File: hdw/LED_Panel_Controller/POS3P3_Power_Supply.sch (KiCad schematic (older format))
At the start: 20 parts

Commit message: made a lot more schematic progress
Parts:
- removed L?: 3.3uH, Inductors_SMD:L_Vishay_IHLP-1212, symbol Custom_Library:L_Custom
- removed U?: TPS62150, Package_DFN_QFN:QFN-16-1EP_3x3mm_P0.5mm_EP1.8x1.8mm, symbol Custom_Library:TPS62150
- added L?: 2.2uH, symbol Custom_Library:L_Custom
- added R? (x3): 0, Resistors_SMD:R_0402, symbol Custom_Library:R_Custom
- added U?: TPS62130, Package_DFN_QFN:QFN-16-1EP_3x3mm_P0.5mm_EP1.8x1.8mm, symbol Custom_Library:TPS62130
- R? (x3): Configuration (none) -> Telemetry
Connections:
- net +12V: now also U?.10 (AVIN), U?.11 (PVIN), U?.12 (PVIN)
- net +3V3: now also R?.2, R?.2, R?.2, U?.14 (VOS)
- net GND: now also U?.15 (PGND), U?.16 (PGND), U?.17 (EP), U?.6 (AGND), U?.7 (FSW), U?.8 (DEF)
- net POS3P3_PGOOD: now also U?.4 (PG)
- net POS3P3_RUN: now also U?.13 (EN)
- net at C?.1, R?.1, R?.2: now also L?.2, R?.1, R?.1, R?.1
- net at R?.1, R?.2: now also U?.5 (FB)
- net at C?.1: now also U?.9 (SS/TR)
- net POS3P3_SNS_OUT+ renamed POS3P3_SNS+
- net POS3P3_SNS_OUT- renamed POS3P3_SNS-
- new net: L?.1, U?.1 (SW), U?.2 (SW), U?.3 (SW)
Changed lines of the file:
@@
 $EndDescr
-$Comp
-L Custom_Library:L_Custom L?
-U 1 1 5C26EF0D
-P 6330 3040
-AR Path="/5CB7718D/5C26EF0D" Ref="L?"  Part="1"
-AR Path="/5E0DC082/5C26EF0D" Ref="L?"  Part="1"
-AR Path="/5E0F263A/5C26EF0D" Ref="L?"  Part="1"
-AR Path="/5EAE2D8A/5C26EF0D" Ref="L?"  Part="1"
-AR Path="/5F581B64/5C26EF0D" Ref="L?"  Part="1"
-F 0 "L?" V 6280 3040 50  0000 C CNN
-F 1 "3.3uH" V 6405 3040 50  0000 C CNN
-F 2 "Inductors_SMD:L_Vishay_IHLP-1212" H 6330 3040 50  0001 C CNN
-F 3 "" H 6330 3040 50  0001 C CNN
-F 4 "541-2567-1-ND" H 6330 3040 50  0001 C CNN "Digi-Key PN"
-F 5 "IHLP1212" V 6480 3040 50  0000 C CNN "display_footprint"
-F 6 "2.7A" V 6580 3040 50  0000 C CNN "Ampacity"
-F 7 "20%" V 6680 3040 50  0000 C CNN "Tolerance"
-	1    6330 3040
-	0    -1   -1   0
-$EndComp
 $Comp
 L Custom_Library:C_Custom C?
@@
 Wire Wire Line
 	5890 3040 6180 3040
-$Comp
-L Custom_Library:R_Custom R?
-U 1 1 5E06F7D6
-P 7520 3040
-AR Path="/5CB6F1ED/5E06F7D6" Ref="R?"  Part="1"
-AR Path="/5CB7718D/5E06F7D6" Ref="R?"  Part="1"
-AR Path="/5E0DC082/5E06F7D6" Ref="R?"  Part="1"
-AR Path="/5E0F263A/5E06F7D6" Ref="R?"  Part="1"
-AR Path="/5EAE2D8A/5E06F7D6" Ref="R?"  Part="1"
-AR Path="/5F581B64/5E06F7D6" Ref="R?"  Part="1"
-F 0 "R?" V 7420 3040 50  0000 C CNN
-F 1 "0.02" V 7520 3040 40  0000 C CNN
-F 2 "Resistors_SMD:R_0612" H 7520 3040 50  0001 C CNN
-F 3 "" H 7520 3040 50  0001 C CNN
-F 4 "P16010CT-ND" H 7820 3440 60  0001 C CNN "Digi-Key PN"
-F 5 "0612" V 7620 3040 50  0000 C CNN "display_footprint"
-F 6 "1%" V 7720 3040 50  0000 C CNN "Tolerance"
-F 7 "1W" V 7820 3040 50  0000 C CNN "Wattage"
-	1    7520 3040
-	0    -1   -1   0
-$EndComp
 Text GLabel 7290 2560 1    50   UnSpc ~ 0
-POS3P3_SNS_OUT+
+POS3P3_SNS+
 Text GLabel 7750 2560 1    50   UnSpc ~ 0
-POS3P3_SNS_OUT-
+POS3P3_SNS-
 Wire Wire Line
 	6480 3040 6920 3040
@@
 F 5 "1%" V 7490 2710 50  0001 C CNN "Tolerance"
 F 6 "1/16W" V 7590 2710 50  0001 C CNN "Wattage"
-F 7 "" H 7290 2710 50  0001 C CNN "Digi-Key PN"
+F 7 "Telemetry" V 7390 2710 50  0000 C CNN "Configuration"
 	1    7290 2710
 	-1   0    0    -1
@@
 F 5 "1%" V 7950 2710 50  0001 C CNN "Tolerance"
 F 6 "1/16W" V 8050 2710 50  0001 C CNN "Wattage"
-F 7 "" H 7750 2710 50  0001 C CNN "Digi-Key PN"
+F 7 "Telemetry" V 7850 2710 50  0000 C CNN "Configuration"
 	1    7750 2710
 	-1   0    0    -1
@@
 Wire Wire Line
 	7290 3040 7370 3040
-Wire Wire Line
-	7750 2860 7750 3040
 Connection ~ 7750 3040
 Wire Wire Line
@@
 	1    0    0    -1
 $EndComp
-$Comp
-L Custom_Library:TPS62150 U?
-U 1 1 5EB8DB31
-P 5390 3740
-F 0 "U?" H 5390 4990 50  0000 C CNN
-F 1 "TPS62150" H 5390 3740 50  0000 C CNN
-F 2 "Package_DFN_QFN:QFN-16-1EP_3x3mm_P0.5mm_EP1.8x1.8mm" H 5390 3740 50  0001 C CNN
-F 3 "https://www.ti.com/lit/ds/symlink/tps62150.pdf?&ts=1589125931316" H 5390 3740 50  0001 C CNN
-F 4 "296-41757-1-ND" H 5290 3740 50  0001 C CNN "Digi-Key PN"
-	1    5390 3740
-	1    0    0    -1
-$EndComp
 Wire Wire Line
 	8220 3960 8220 4240
@@
 Text GLabel 4090 7490 0    50   Input ~ 0
 POS3P3_RUN
+$Comp
+L Custom_Library:TPS62130 U?
+U 1 1 6019E970
+P 5390 3740
+AR Path="/5F581BA3/6019E970" Ref="U?"  Part="1"
+AR Path="/5F581B64/6019E970" Ref="U?"  Part="1"
+F 0 "U?" H 5390 4990 50  0000 C CNN
+F 1 "TPS62130" H 5390 3740 50  0000 C CNN
+F 2 "Package_DFN_QFN:QFN-16-1EP_3x3mm_P0.5mm_EP1.8x1.8mm" H 5390 3740 50  0001 C CNN
+F 3 "http://www.ti.com/lit/ds/symlink/tps62130.pdf" H 5390 3740 50  0001 C CNN
+F 4 "296-37878-1-ND" H 5290 3740 50  0001 C CNN "Digi-Key PN"
+	1    5390 3740
+	1    0    0    -1
+$EndComp
+$Comp
+L Custom_Library:L_Custom L?
+U 1 1 601A324F
+P 6330 3040
+AR Path="/5F581BA3/601A324F" Ref="L?"  Part="1"
+AR Path="/5F581B64/601A324F" Ref="L?"  Part="1"
+F 0 "L?" V 6280 3040 50  0000 C CNN
+F 1 "2.2uH" V 6405 3040 50  0000 C CNN
+F 2 "" H 6330 3040 50  0001 C CNN
+F 3 "" H 6330 3040 50  0001 C CNN
+F 4 "IHLP2020" V 6480 3040 50  0000 C CNN "display_footprint"
+F 5 "6.7A" V 6580 3040 50  0000 C CNN "Ampacity"
+F 6 "20%" V 6680 3040 50  0000 C CNN "Tolerance"
+F 7 "541-1236-1-ND" H 6330 3040 50  0001 C CNN "Digi-Key PN"
+	1    6330 3040
+	0    -1   -1   0
+$EndComp
+$Comp
+L Custom_Library:R_Custom R?
+U 1 1 601AAF61
+P 7520 3410
+AR Path="/5EAE2EF2/601AAF61" Ref="R?"  Part="1"
+AR Path="/5EAE30C7/601AAF61" Ref="R?"  Part="1"
+AR Path="/5EAE2D8A/601AAF61" Ref="R?"  Part="1"
+AR Path="/5EAE2D66/601AAF61" Ref="R?"  Part="1"
+AR Path="/5F581B41/601AAF61" Ref="R?"  Part="1"
+AR Path="/5F581B64/601AAF61" Ref="R?"  Part="1"
+F 0 "R?" V 7420 3410 50  0000 C CNN
+F 1 "0" V 7520 3410 50  0000 C CNN
+F 2 "Resistors_SMD:R_0402" H 7520 3410 50  0001 C CNN
+F 3 "" H 7520 3410 50  0001 C CNN
+F 4 "0402" V 7620 3410 50  0001 C CNN "display_footprint"
+F 5 "1%" V 7720 3410 50  0001 C CNN "Tolerance"
+F 6 "1/16W" V 7820 3410 50  0001 C CNN "Wattage"
+F 7 "~Telemetry" V 7620 3410 50  0000 C CNN "Configuration"
+F 8 "2019-RK73Z1ETTPCT-ND" H 7520 3410 50  0001 C CNN "Digi-Key PN"
+	1    7520 3410
+	0    -1   1    0
+$EndComp
+$Comp
+L Custom_Library:R_Custom R?
+U 1 1 601AAF6C
+P 7520 3710
+AR Path="/5EAE2EF2/601AAF6C" Ref="R?"  Part="1"
+AR Path="/5EAE30C7/601AAF6C" Ref="R?"  Part="1"
+AR Path="/5EAE2D8A/601AAF6C" Ref="R?"  Part="1"
+AR Path="/5EAE2D66/601AAF6C" Ref="R?"  Part="1"
+AR Path="/5F581B41/601AAF6C" Ref="R?"  Part="1"
+AR Path="/5F581B64/601AAF6C" Ref="R?"  Part="1"
+F 0 "R?" V 7420 3710 50  0000 C CNN
+F 1 "0" V 7520 3710 50  0000 C CNN
+F 2 "Resistors_SMD:R_0402" H 7520 3710 50  0001 C CNN
+F 3 "" H 7520 3710 50  0001 C CNN
+F 4 "0402" V 7620 3710 50  0001 C CNN "display_footprint"
+F 5 "1%" V 7720 3710 50  0001 C CNN "Tolerance"
+F 6 "1/16W" V 7820 3710 50  0001 C CNN "Wattage"
+F 7 "~Telemetry" V 7620 3710 50  0000 C CNN "Configuration"
+F 8 "2019-RK73Z1ETTPCT-ND" H 7520 3710 50  0001 C CNN "Digi-Key PN"
+	1    7520 3710
+	0    -1   1    0
+$EndComp
+$Comp
+L Custom_Library:R_Custom R?
+U 1 1 601AAF77
+P 7520 4010
+AR Path="/5EAE2EF2/601AAF77" Ref="R?"  Part="1"
+AR Path="/5EAE30C7/601AAF77" Ref="R?"  Part="1"
+AR Path="/5EAE2D8A/601AAF77" Ref="R?"  Part="1"
+AR Path="/5EAE2D66/601AAF77" Ref="R?"  Part="1"
+AR Path="/5F581B41/601AAF77" Ref="R?"  Part="1"
+AR Path="/5F581B64/601AAF77" Ref="R?"  Part="1"
+F 0 "R?" V 7420 4010 50  0000 C CNN
+F 1 "0" V 7520 4010 50  0000 C CNN
+F 2 "Resistors_SMD:R_0402" H 7520 4010 50  0001 C CNN
+F 3 "" H 7520 4010 50  0001 C CNN
+F 4 "0402" V 7620 4010 50  0001 C CNN "display_footprint"
+F 5 "1%" V 7720 4010 50  0001 C CNN "Tolerance"
+F 6 "1/16W" V 7820 4010 50  0001 C CNN "Wattage"
+F 7 "~Telemetry" V 7620 4010 50  0000 C CNN "Configuration"
+F 8 "2019-RK73Z1ETTPCT-ND" H 7520 4010 50  0001 C CNN "Digi-Key PN"
+	1    7520 4010
+	0    -1   1    0
+$EndComp
+Wire Wire Line
+	7670 4010 7750 4010
+Wire Wire Line
+	7750 4010 7750 3710
+Wire Wire Line
+	7290 4010 7370 4010
+Wire Wire Line
+	7370 3710 7290 3710
+Connection ~ 7290 3710
+Wire Wire Line
+	7290 3710 7290 4010
+Wire Wire Line
+	7670 3710 7750 3710
+Connection ~ 7750 3710
+Wire Wire Line
+	7750 3710 7750 3410
+Wire Wire Line
+	7670 3410 7750 3410
+Connection ~ 7750 3410
+Wire Wire Line
+	7370 3410 7290 3410
+Connection ~ 7290 3410
+Wire Wire Line
+	7290 3410 7290 3710
+Wire Wire Line
+	7750 2860 7750 3040
+$Comp
+L Custom_Library:R_Custom R?
+U 1 1 5E06F7D6
+P 7520 3040
+AR Path="/5CB6F1ED/5E06F7D6" Ref="R?"  Part="1"
+AR Path="/5CB7718D/5E06F7D6" Ref="R?"  Part="1"
+AR Path="/5E0DC082/5E06F7D6" Ref="R?"  Part="1"
+AR Path="/5E0F263A/5E06F7D6" Ref="R?"  Part="1"
+AR Path="/5EAE2D8A/5E06F7D6" Ref="R?"  Part="1"
+AR Path="/5F581B64/5E06F7D6" Ref="R?"  Part="1"
+F 0 "R?" V 7420 3040 50  0000 C CNN
+F 1 "0.02" V 7520 3040 40  0000 C CNN
+F 2 "Resistors_SMD:R_0612" H 7520 3040 50  0001 C CNN
+F 3 "" H 7520 3040 50  0001 C CNN
+F 4 "P16010CT-ND" H 7820 3440 60  0001 C CNN "Digi-Key PN"
+F 5 "0612" V 7620 3040 50  0000 C CNN "display_footprint"
+F 6 "1%" V 7720 3040 50  0000 C CNN "Tolerance"
+F 7 "1W" V 7820 3040 50  0000 C CNN "Wattage"
+F 8 "Telemetry" V 7350 3040 50  0000 C CNN "Configuration"
+	1    7520 3040
+	0    -1   -1   0
+$EndComp
+Wire Wire Line
+	7290 3040 7290 3410
+Wire Wire Line
+	7750 3040 7750 3410
 $EndSCHEMATC

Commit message: more schematic development
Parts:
- removed C?: 100uF, Capacitors_SMD:C_1206, symbol Custom_Library:C_Custom
- removed C?: 0.1uF, Capacitors_SMD:C_0402, symbol Custom_Library:C_Custom
- removed C?: 10uF, Capacitors_SMD:C_0402, symbol Custom_Library:C_Custom
- removed D?: BAT48JFILM, Diode_SMD:D_SOD-323, symbol Diode:BAT48JFILM
- removed L?: 2.2uH, symbol Custom_Library:L_Custom
- removed Q?: ZXMS6004FFTA, Package_TO_SOT_SMD:SOT-23, symbol Custom_Library:ZXMS6004FFTA
- removed Q?: BSS214NW, Package_TO_SOT_SMD:SOT-323_SC-70, symbol Transistor_FET:BSS214NW
- removed R?: 10k, Resistors_SMD:R_0402, symbol Custom_Library:R_Custom
- removed R?: 10, Resistors_SMD:R_0402, symbol Custom_Library:R_Custom
- removed R? (x3): 0, Resistors_SMD:R_0402, symbol Custom_Library:R_Custom
- removed U?: TPS62130, Package_DFN_QFN:QFN-16-1EP_3x3mm_P0.5mm_EP1.8x1.8mm, symbol Custom_Library:TPS62130
- added C?: 0.1uF, Capacitors_SMD:C_0402, symbol Custom_Library:C_Custom
- added C? (x2): 10uF, Capacitors_SMD:C_1206, symbol Custom_Library:C_Custom
- added C?: 10uF, Capacitors_SMD:C_0402, symbol Custom_Library:C_Custom
- added D?: BAT48JFILM, Diode_SMD:D_SOD-323, symbol Diode:BAT48JFILM
- added L?: 3.3uH, Inductors_SMD:L_Vishay_IHLP-1212, symbol Custom_Library:L_Custom
- added Q?: ZXMS6004FFTA, Package_TO_SOT_SMD:SOT-23, symbol Custom_Library:ZXMS6004FFTA
- added Q?: BSS214NW, Package_TO_SOT_SMD:SOT-323_SC-70, symbol Transistor_FET:BSS214NW
- added R? (x5): 0, Resistors_SMD:R_0402, symbol Custom_Library:R_Custom
- added R? (x2): 10k, Resistors_SMD:R_0402, symbol Custom_Library:R_Custom
- added U?: TPS62152, Package_DFN_QFN:QFN-16-1EP_3x3mm_P0.5mm_EP1.8x1.8mm, symbol Custom_Library:TPS62150
- added U?: 74LVC1G97, Package_TO_SOT_SMD:SOT-363_SC-70-6, symbol Custom_Library:74LVC1G97_Power_AND
- C?: Dielectric X7R -> X5R; Digi-Key PN 1276-7031-1-ND -> 1276-1181-1-ND
- C?: Digi-Key PN (none) -> 490-10698-1-ND; Voltage 50V -> 25V
- C?: Digi-Key PN 490-13295-1-ND -> 399-3066-1-ND; display_footprint (none) -> 0402
- R?: Configuration (none) -> DNP; Digi-Key PN (none) -> RMCF0402FT562KCT-ND
- R?: Configuration (none) -> DNP; Digi-Key PN (none) -> RMCF0402FT180KCT-ND
- R? (x2): Digi-Key PN (none) -> RMCF0402FT10R0CT-ND
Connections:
- net +12V: now also U?.10 (AVIN), U?.11 (PVIN), U?.12 (PVIN)
- net +3V3: now also C?.1, D?.2 (A), Q?.3 (D), R?.2, R?.2, R?.2, U?.14 (VOS), U?.5 (VCC)
- net GND: now also C?.2, C?.2, C?.2, C?.2, Q?.2 (S), Q?.2 (S), R?.2, R?.2, U?.1 (GND), U?.15 (PGND), U?.16 (PGND), U?.17 (EP), U?.2 (GND), U?.6 (AGND), U?.7 (FSW), U?.8 (DEF)
- net POS12_PGOOD: now also R?.1
- net POS3P3_PGOOD: now also R?.1, U?.4; no longer R?.2
- net POS3P3_RUN: now also Q?.1 (G), R?.2, U?.13 (EN), U?.3
- net at R?.1, R?.2: now also C?.1, C?.1, L?.2, R?.1, R?.1, R?.1
- net at R?.1, R?.2: now also R?.1, U?.5 (FB)
- net at C?.1: now also U?.9 (SS/TR)
- new net: L?.1, U?.1 (SW), U?.2 (SW), U?.3 (SW)
- new net: R?.2, U?.4 (PG), U?.6
- new net: Q?.1 (G), Q?.3 (D), R?.2
- new net: C?.1, D?.1 (K), R?.1
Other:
- note added: "Fixed VOUT = +3.3V"
- moved on the sheet: R?, TP?

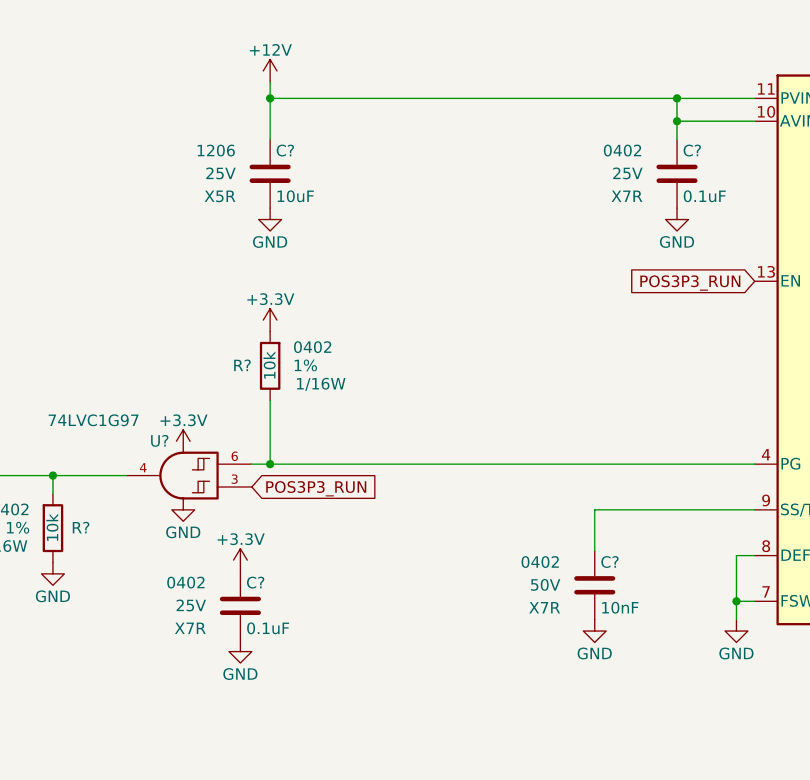
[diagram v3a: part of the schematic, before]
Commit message: added digikey pns, footprints, bom scrubbed
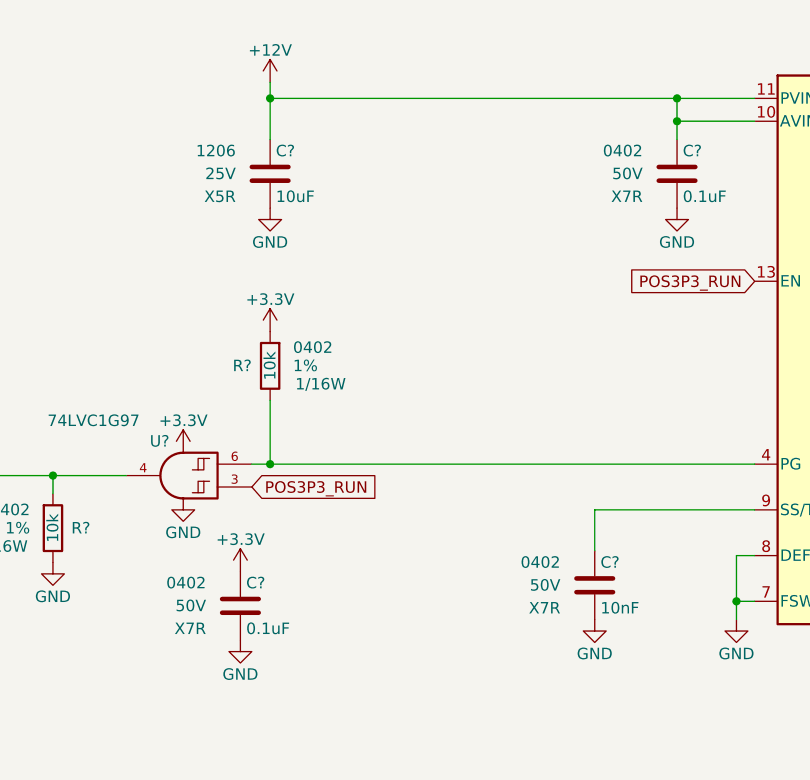
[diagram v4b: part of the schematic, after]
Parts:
- C? (x3): Digi-Key PN 1276-1181-1-ND -> 399-8153-1-ND
- C? (x2): Digi-Key PN 490-10698-1-ND -> 490-10701-1-ND; Voltage 25V -> 50V
- C?: Digi-Key PN 490-13211-1-ND -> 1276-1451-1-ND
- R? (x5): Digi-Key PN 2019-RK73Z1ETTPCT-ND -> RMCF0402ZT0R00CT-ND
- U?: Digi-Key PN 296-SN74LVC1G97DCK3CT-ND -> 1727-1772-1-ND
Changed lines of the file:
@@
 F 3 "" H 4575 3070 50  0001 C CNN
 F 4 "0402" H 4400 3070 50  0000 R CNN "display_footprint"
-F 5 "25V" H 4400 2970 50  0000 R CNN "Voltage"
+F 5 "50V" H 4400 2970 50  0000 R CNN "Voltage"
 F 6 "X7R" H 4400 2870 50  0000 R CNN "Dielectric"
-F 7 "490-10698-1-ND" H 4550 2970 50  0001 C CNN "Digi-Key PN"
+F 7 "490-10701-1-ND" H 4550 2970 50  0001 C CNN "Digi-Key PN"
 	1    4550 2970
 	1    0    0    -1
@@
 F 5 "25V" H 2620 2970 50  0000 R CNN "Voltage"
 F 6 "X5R" H 2620 2870 50  0000 R CNN "Dielectric"
-F 7 "1276-1181-1-ND" H 3195 3470 60  0001 C CNN "Digi-Key PN"
+F 7 "399-8153-1-ND" H 3195 3470 60  0001 C CNN "Digi-Key PN"
 	1    2770 2970
 	1    0    0    -1
@@
 F 5 "1%" V 2040 6470 50  0000 C CNN "Tolerance"
 F 6 "1/16W" V 2140 6470 50  0000 C CNN "Wattage"
-F 7 "2019-RK73Z1ETTPCT-ND" H 1840 6470 50  0001 C CNN "Digi-Key PN"
+F 7 "RMCF0402ZT0R00CT-ND" H 1840 6470 50  0001 C CNN "Digi-Key PN"
 	1    1840 6470
 	0    -1   1    0
@@
 F 2 "Package_TO_SOT_SMD:SOT-363_SC-70-6" H 2440 4290 50  0001 C CNN
 F 3 "http://www.ti.com/lit/ds/symlink/sn74lvc1g97.pdf" H 2440 4290 50  0001 C CNN
-F 4 "296-SN74LVC1G97DCK3CT-ND" H 2390 4290 50  0001 C CNN "Digi-Key PN"
+F 4 "1727-1772-1-ND" H 2390 4290 50  0001 C CNN "Digi-Key PN"
 	1    2390 4290
 	-1   0    0    -1
@@
 F 3 "" H 2665 4960 50  0001 C CNN
 F 4 "0402" H 2490 4960 50  0000 R CNN "display_footprint"
-F 5 "25V" H 2490 4860 50  0000 R CNN "Voltage"
+F 5 "50V" H 2490 4860 50  0000 R CNN "Voltage"
 F 6 "X7R" H 2490 4760 50  0000 R CNN "Dielectric"
-F 7 "490-10698-1-ND" H 2640 4860 50  0001 C CNN "Digi-Key PN"
+F 7 "490-10701-1-ND" H 2640 4860 50  0001 C CNN "Digi-Key PN"
 	1    2640 4860
 	1    0    0    -1
@@
 F 5 "1%" H 7310 4720 50  0000 R CNN "Tolerance"
 F 6 "1/16W" H 7310 4620 50  0000 R CNN "Wattage"
-F 7 "2019-RK73Z1ETTPCT-ND" H 7410 4720 50  0001 C CNN "Digi-Key PN"
+F 7 "RMCF0402ZT0R00CT-ND" H 7410 4720 50  0001 C CNN "Digi-Key PN"
 	1    7410 4720
 	-1   0    0    -1
@@
 F 6 "1/16W" V 8310 3450 50  0001 C CNN "Wattage"
 F 7 "~Telemetry" V 8110 3450 50  0000 C CNN "Configuration"
-F 8 "2019-RK73Z1ETTPCT-ND" H 8010 3450 50  0001 C CNN "Digi-Key PN"
+F 8 "RMCF0402ZT0R00CT-ND" H 8010 3450 50  0001 C CNN "Digi-Key PN"
 	1    8010 3450
 	0    -1   1    0
@@
 F 6 "1/16W" V 8310 3750 50  0001 C CNN "Wattage"
 F 7 "~Telemetry" V 8110 3750 50  0000 C CNN "Configuration"
-F 8 "2019-RK73Z1ETTPCT-ND" H 8010 3750 50  0001 C CNN "Digi-Key PN"
+F 8 "RMCF0402ZT0R00CT-ND" H 8010 3750 50  0001 C CNN "Digi-Key PN"
 	1    8010 3750
 	0    -1   1    0
@@
 F 6 "1/16W" V 8310 4050 50  0001 C CNN "Wattage"
 F 7 "~Telemetry" V 8110 4050 50  0000 C CNN "Configuration"
-F 8 "2019-RK73Z1ETTPCT-ND" H 8010 4050 50  0001 C CNN "Digi-Key PN"
+F 8 "RMCF0402ZT0R00CT-ND" H 8010 4050 50  0001 C CNN "Digi-Key PN"
 	1    8010 4050
 	0    -1   1    0
@@
 F 5 "25V" H 7260 3280 50  0000 R CNN "Voltage"
 F 6 "X5R" H 7260 3180 50  0000 R CNN "Dielectric"
-F 7 "1276-1181-1-ND" H 7835 3780 60  0001 C CNN "Digi-Key PN"
+F 7 "399-8153-1-ND" H 7835 3780 60  0001 C CNN "Digi-Key PN"
 	1    7410 3280
 	1    0    0    -1
@@
 F 5 "25V" H 6670 3280 50  0000 R CNN "Voltage"
 F 6 "X5R" H 6670 3180 50  0000 R CNN "Dielectric"
-F 7 "1276-1181-1-ND" H 7245 3780 60  0001 C CNN "Digi-Key PN"
+F 7 "399-8153-1-ND" H 7245 3780 60  0001 C CNN "Digi-Key PN"
 	1    6820 3280
 	1    0    0    -1
@@
 F 5 "6.3V" H 3320 6860 50  0000 R CNN "Voltage"
 F 6 "X5R" H 3320 6760 50  0000 R CNN "Dielectric"
-F 7 "490-13211-1-ND" H 3470 6860 50  0001 C CNN "Digi-Key PN"
+F 7 "1276-1451-1-ND" H 3470 6860 50  0001 C CNN "Digi-Key PN"
 	1    3470 6860
 	1    0    0    -1
